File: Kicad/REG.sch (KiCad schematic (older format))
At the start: 6 parts, among them U27 74HCT377, U28 74HCT244, U29 74HCT161, U30 74HCT161, U31 74HCT377, U37 74HCT377

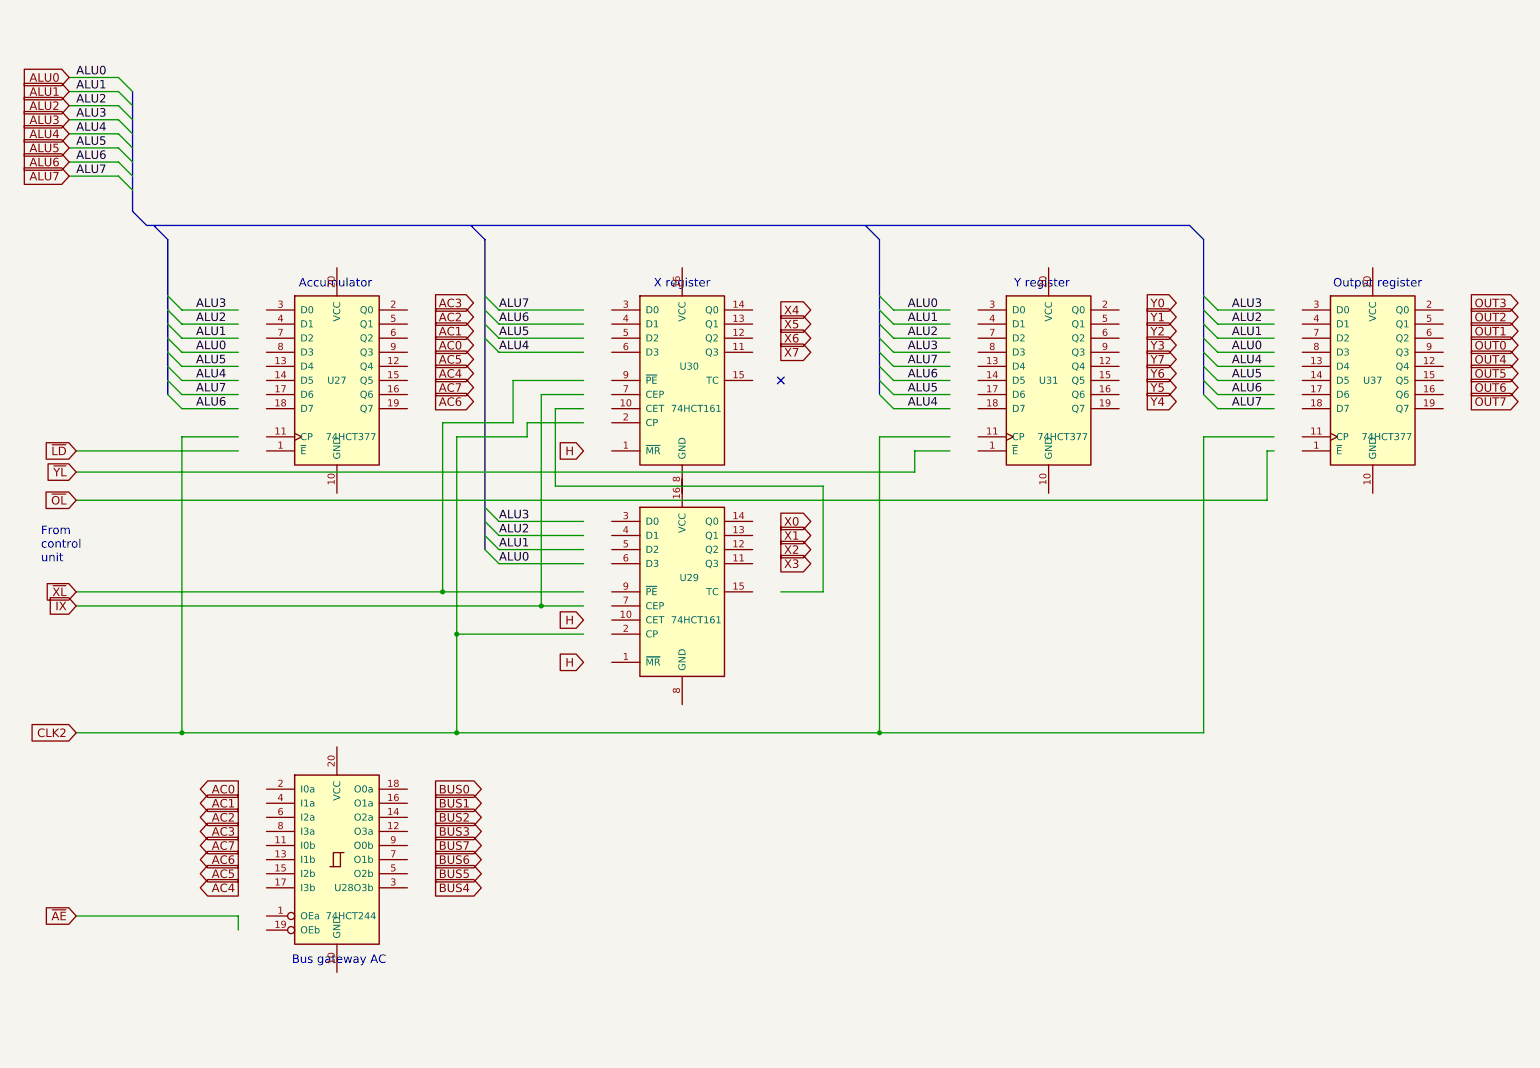
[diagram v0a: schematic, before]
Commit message: Update to work with mostly the default KiCAD items or items downloaded via the KiCAD Libraries too.
2 Resistors added of 1k on the lines for TRUE and FALSE pull ups.

Several things deleted which appeared at Graphic shapes on the PCB sometimes
but could not be edited. this was done manually at the bottom of the PCB_KiCAD file.

Deleted some PCB items around the order which marked the Copper limits of top and bottom. may have been tied to TRUE & FALSE.

Changed USB socket type.

This has been done not to change the board but to aid understanding and allow anyone who wants slightly easier access.

I have not tested it and provide no warranty.

Signed-off-by: John Bradley <flypie@rocketmail.com>
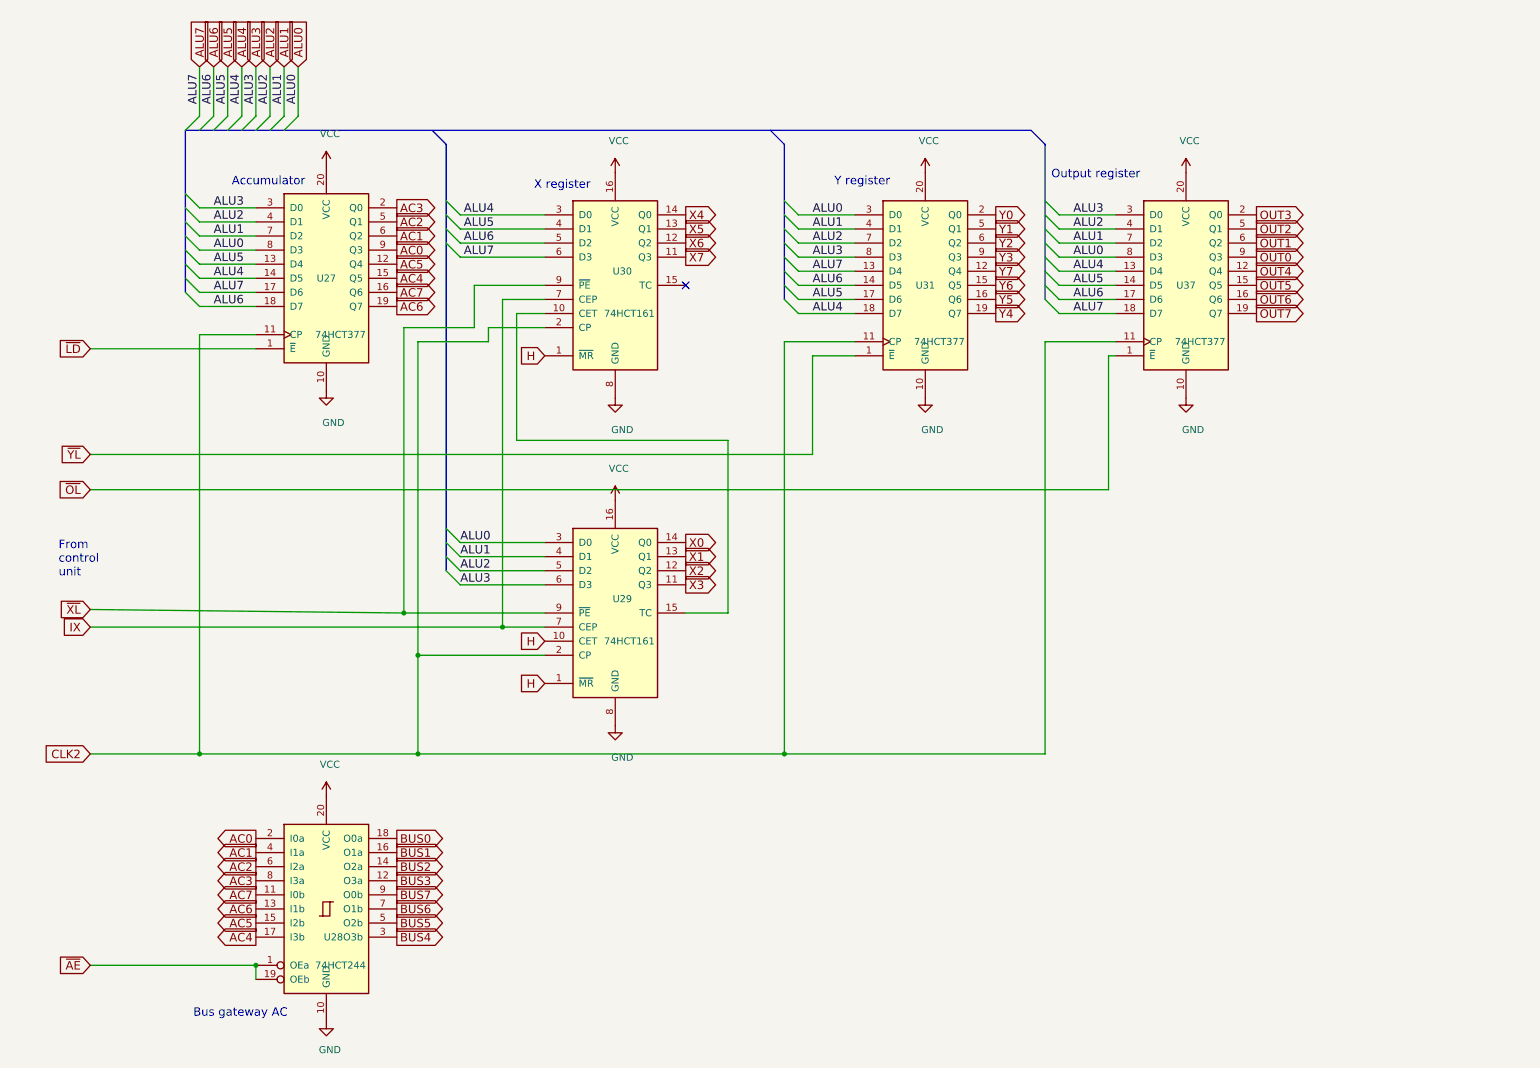
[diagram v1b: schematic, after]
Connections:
- net labels added: GND, VCC
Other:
- moved on the sheet: U27, U28, U29, U30, U31, U37
